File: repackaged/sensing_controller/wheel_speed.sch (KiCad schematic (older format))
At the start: 39 parts, among them J1 CONN_02X03, U1 MCP2561-E_SN, U101 TPS560430YF, U2 ATMEGA16M1, Y1 Crystal_SMD

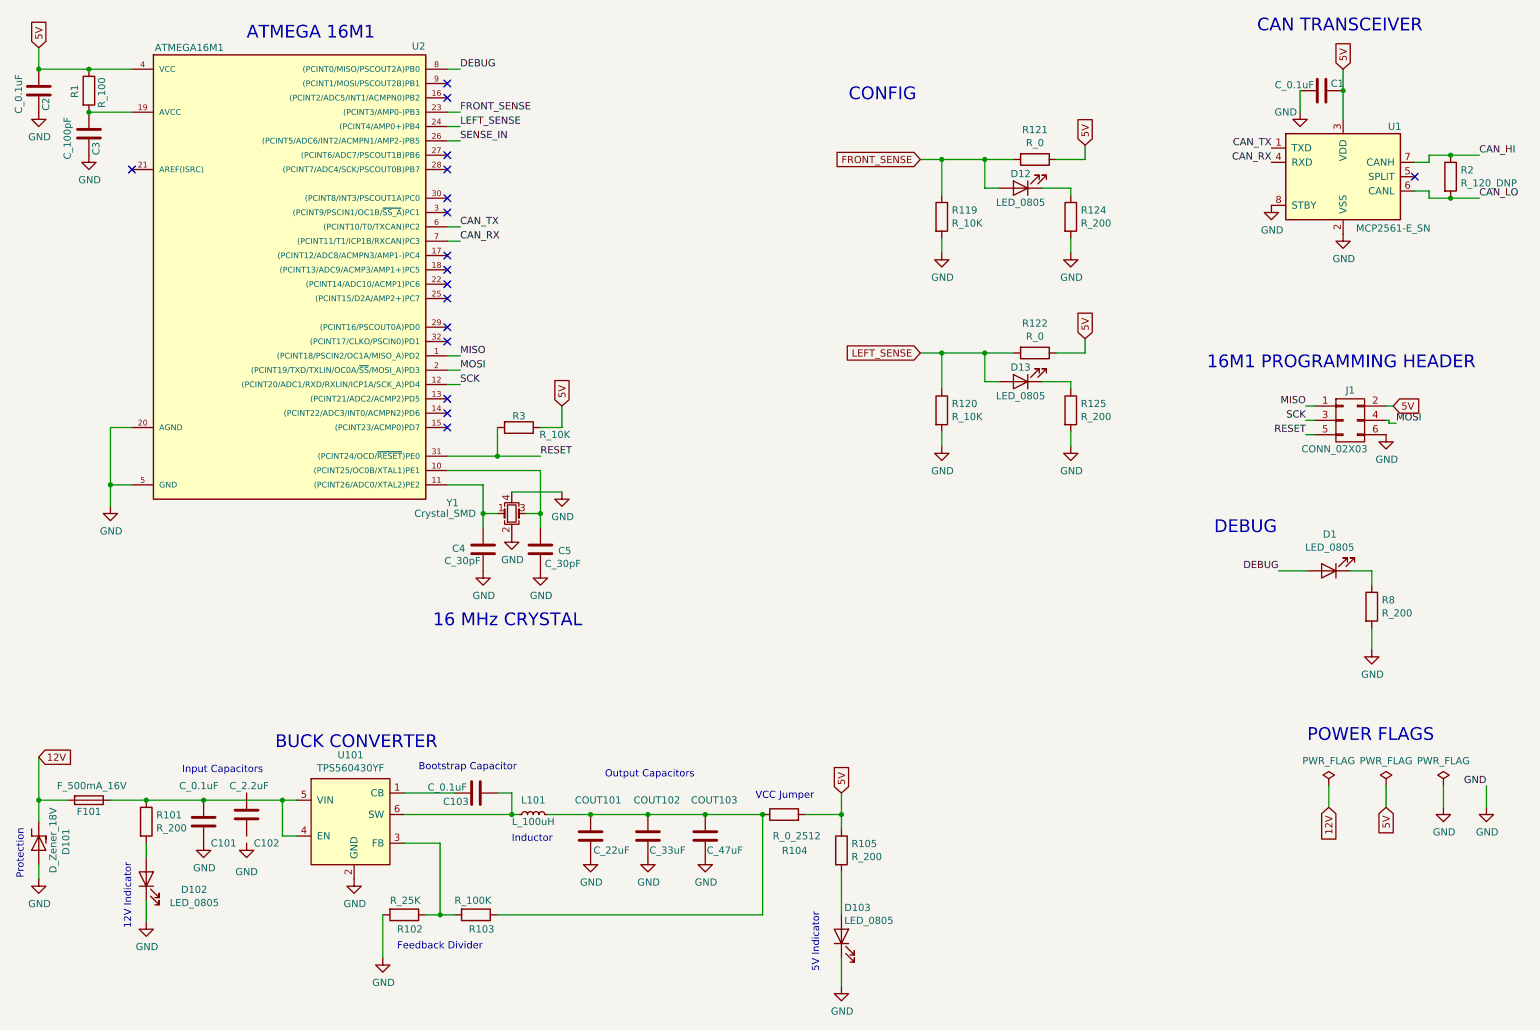
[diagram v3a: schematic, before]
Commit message: moved all circuitry to 50mil grid, fixed net labels, fixed footprints, added connectors
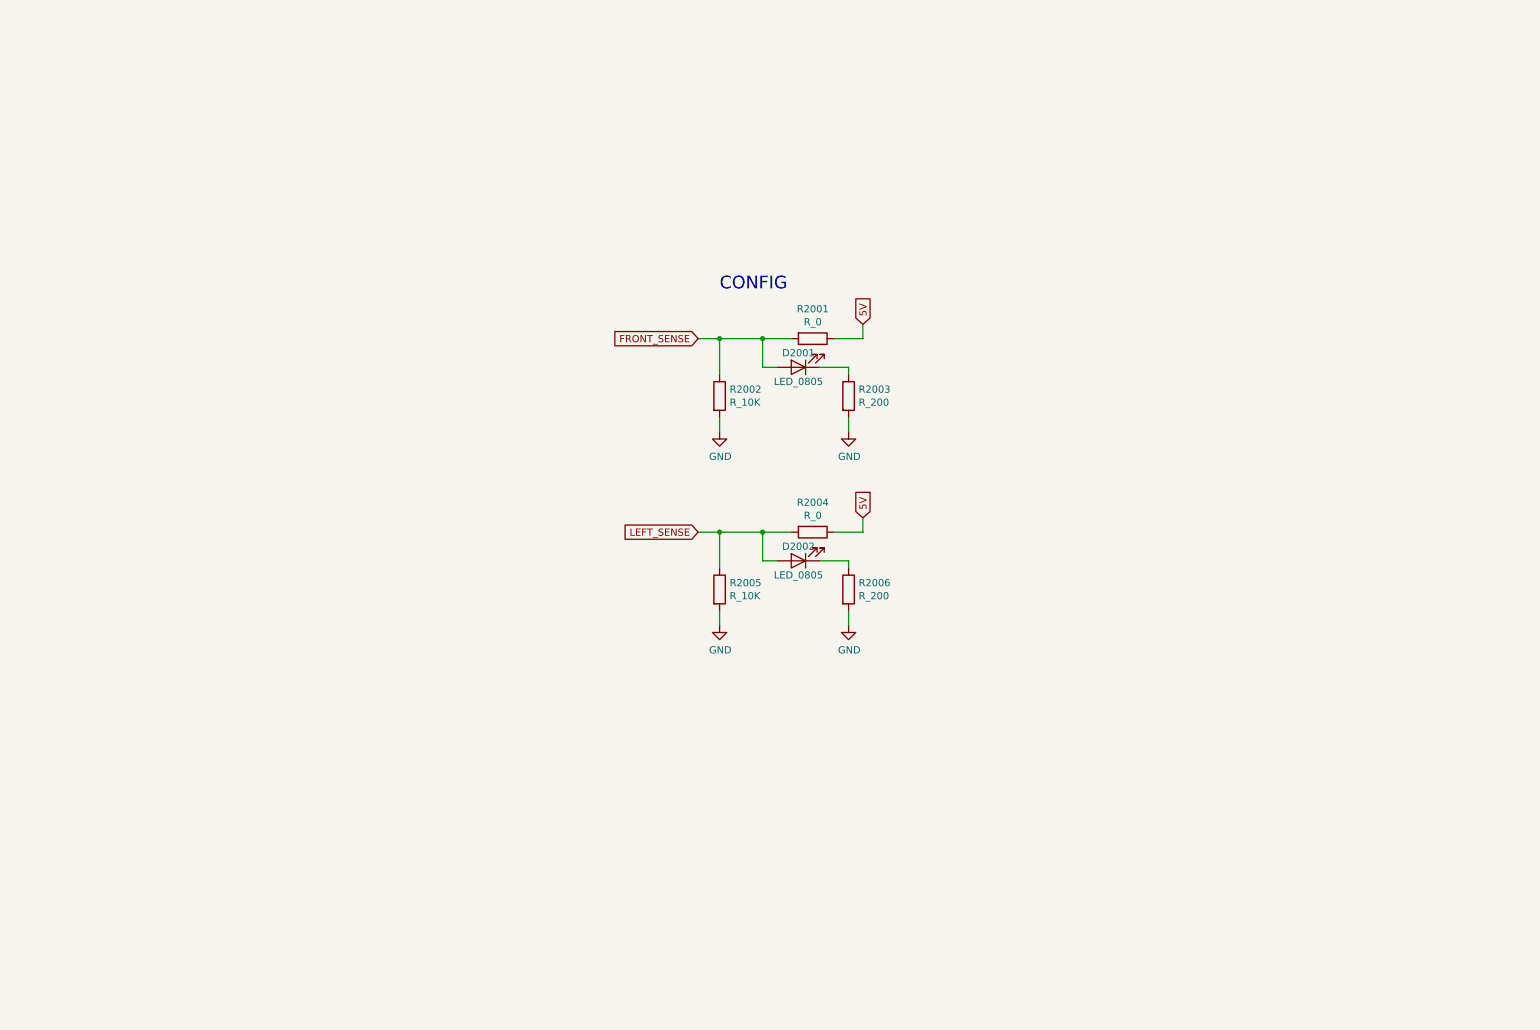
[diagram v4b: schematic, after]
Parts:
- removed C1, C101, C103, C2: C_0.1uF, footprints:C_0805_OEM, symbol formula:C_0.1uF
- removed C102: C_2.2uF, footprints:C_0603_1608Metric, symbol formula:C_2.2uF
- removed C3: C_100pF, footprints:C_0805_OEM, symbol formula:C_100pF
- removed C4, C5: C_30pF, footprints:C_0805_OEM, symbol formula:C_30pF
- removed COUT101: C_22uF, footprints:C_1206_OEM, symbol formula:C_22uF
- removed COUT102: C_33uF, footprints:C_1812_OEM, symbol formula:C_33uF
- removed COUT103: C_47uF, footprints:C_0805_OEM, symbol formula:C_47uF
- removed D1, D102, D103: LED_0805, footprints:LED_0805_OEM, symbol formula:LED_0805
- removed D101: D_Zener_18V, footprints:DO-214AA, symbol formula:D_Zener_18V
- removed F101: F_500mA_16V, footprints:Fuse_1210, symbol formula:F_500mA_16V
- removed J1: CONN_02X03, footprints:Pin_Header_Straight_2x03, symbol formula:CONN_02X03
- removed L101: L_100uH, formula:L_100uH, symbol formula:L_100uH
- removed R1: R_100, footprints:R_0805_OEM, symbol formula:R_100
- removed R101, R105, R8: R_200, footprints:R_0805_OEM, symbol formula:R_200
- removed R102: R_25K, footprints:R_0805_OEM, symbol formula:R_25K
- removed R103: R_100K, footprints:R_0805_OEM, symbol formula:R_100K
- removed R104: R_0_2512, footprints:R_2512_OEM, symbol formula:R_0_2512
- removed R2: R_120_DNP, footprints:R_0805_OEM, symbol formula:R_120_DNP
- removed R3: R_10K, footprints:R_0805_OEM, symbol formula:R_10K
- removed U1: MCP2561-E_SN, footprints:SOIC-8_3.9x4.9mm_Pitch1.27mm_OEM, symbol formula:MCP2561-E_SN
- removed U101: TPS560430YF, Package_TO_SOT_SMD:SOT-23-6_Handsoldering, symbol formula:TPS560430YF
- removed U2: ATMEGA16M1, footprints:TQFP-32_7x7mm_Pitch0.8mm, symbol formula:ATMEGA16M1
- removed Y1: Crystal_SMD, footprints:Crystal_SMD_FA238, symbol formula:Crystal_SMD
- renumbered D12 to D2001, D13 to D2002, R121 to R2001, R119 to R2002, R124 to R2003, R122 to R2004, R120 to R2005, R125 to R2006
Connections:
- no-connect marks 17 -> 0
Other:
- note removed: "12V Indicator"
- note removed: "16 MHz CRYSTAL\n"
- note removed: "16M1 PROGRAMMING HEADER\n"
- note removed: "5V Indicator"
- note removed: "ATMEGA 16M1\n"
- note removed: "BUCK CONVERTER\n"
- note removed: "Bootstrap Capacitor\n"
- note removed: "CAN TRANSCEIVER\n"
- note removed: "DEBUG"
- note removed: "Feedback Divider\n"
- note removed: "Inductor\n"
- note removed: "Input Capacitors\n\n"
- note removed: "Output Capacitors\n"
- note removed: "POWER FLAGS\n"
- note removed: "Protection\n"
- note removed: "VCC Jumper\n"
- moved on the sheet: D2001, D2002, R2001, R2002, R2003, R2004, R2005, R2006
